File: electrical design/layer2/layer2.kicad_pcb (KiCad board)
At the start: 2 copper layers, 178 x 168.1 mm, 43 parts, among them J1 Conn_01x01_Female, J10 Conn_01x01_Female, J11 SH1.0 2P, J12 XT60-F, J13 XT60-F, J14 XH2.54 2P, J15 XT60-F, J16 XT60-F, J17 SH1.0 2P, J2 Conn_01x01_Female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

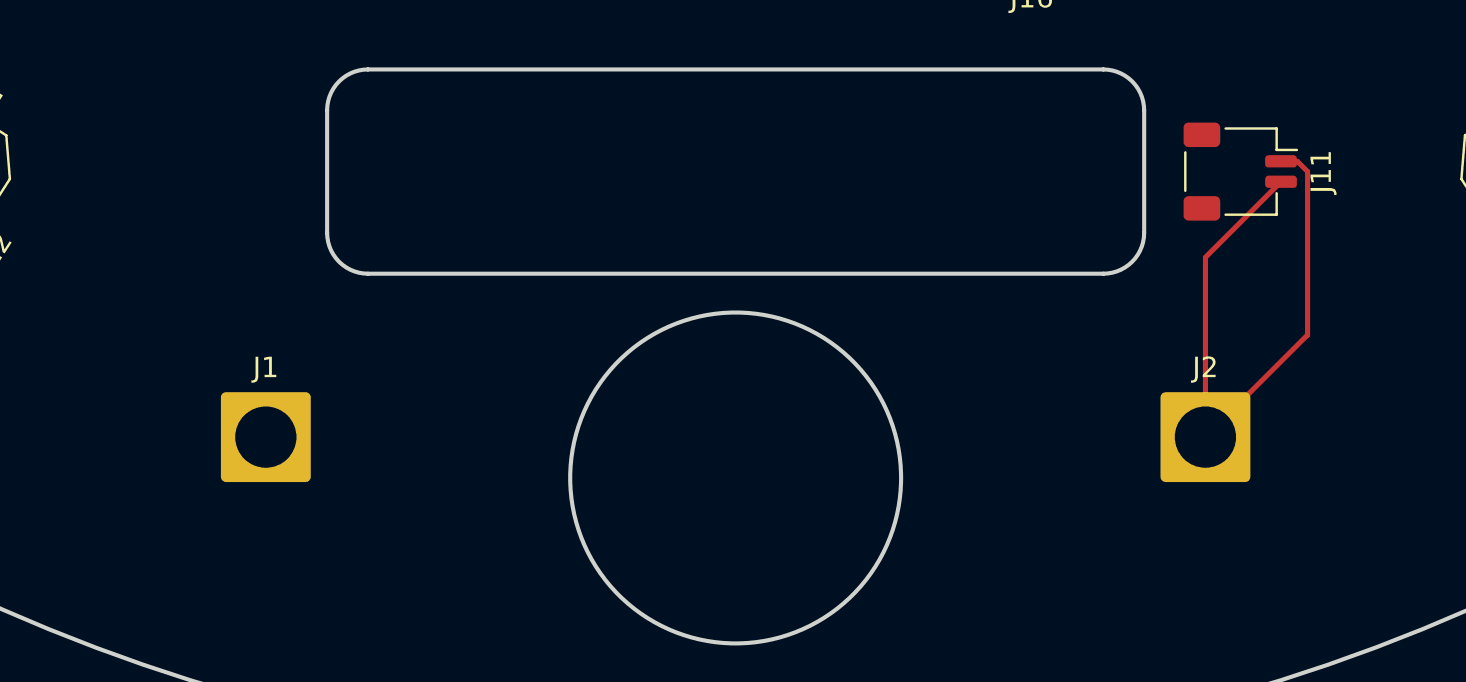
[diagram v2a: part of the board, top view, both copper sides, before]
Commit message: update l2 pcb with additional batt connectors
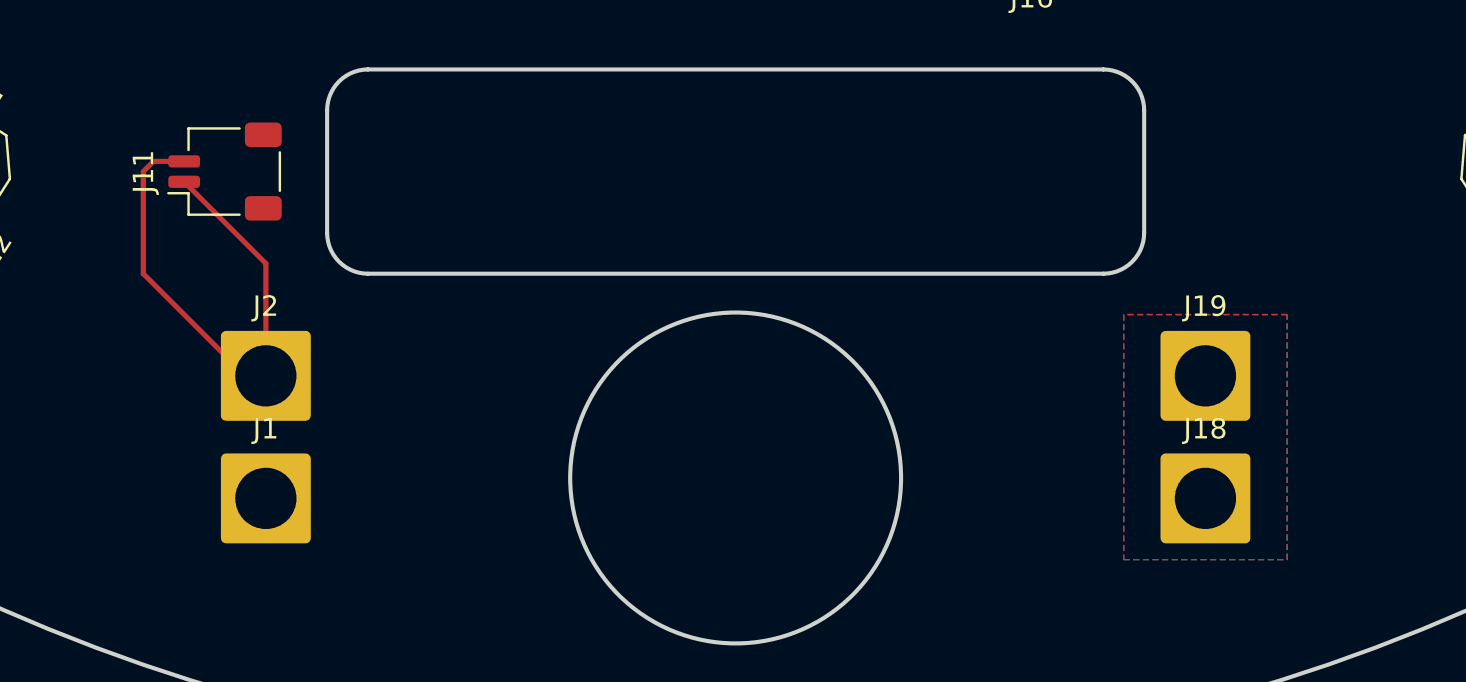
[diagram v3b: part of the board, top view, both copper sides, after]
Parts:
- added J18: Conn_01x01_Female, Connector_Wire:SolderWire-2.5sqmm_1x01_D2.4mm_OD4.4mm, F.Cu at (128.0, 181.0)
- added J19: Conn_01x01_Female, Connector_Wire:SolderWire-2.5sqmm_1x01_D2.4mm_OD4.4mm, F.Cu at (128.0, 175.0)
- moved J11 49.7 mm to (80.0, 165.0), turned to 90 degrees
- moved J2 46.1 mm to (82.0, 175.0)
- moved J1 3.00 mm to (82.0, 181.0)
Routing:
- net GND: track 32.0 -> 26.4 mm
- added copper zone on B.Cu, net /BATT
- added copper zone on F.Cu, net /BATT
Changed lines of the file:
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@@
   (net 1 "+12V")
   (net 2 "GND")
+  (net 3 "/BATT")
   (footprint "Connector_AMASS:AMASS_XT30UPB-F_1x02_P5.0mm_Vertical" (layer "F.Cu")
     (at 143.357043 164.747279 -57.3)
@@
   )
   (footprint "Connector_Wire:SolderWire-2.5sqmm_1x01_D2.4mm_OD4.4mm" (layer "F.Cu")
-    (at 128 178)
+    (at 128 181)
+    (descr "Soldered wire connection, for a single 2.5 mm² wire, reinforced insulation, conductor diameter 2.4mm, outer diameter 4.4mm, size source Multi-Contact FLEXI-xV 2.5 (https://ec.staubli.com/AcroFiles/Catalogues/TM_Cab-Main-11014119_(en)_hi.pdf), bend radius 3 times outer diameter, generated with kicad-footprint-generator")
+    (tags "connector wire 2.5sqmm")
+    (property "Sheetfile" "layer2.kicad_sch")
+    (property "Sheetname" "")
+    (property "ki_description" "Generic connector, single row, 01x01, script generated (kicad-library-utils/schlib/autogen/connector/)")
+    (property "ki_keywords" "connector")
+    (attr exclude_from_pos_files)
+    (fp_text reference "J18" (at 0 -3.4) (layer "F.SilkS")
+        (effects (font (size 1 1) (thickness 0.15)))
+    )
+    (fp_text value "Conn_01x01_Female" (at 0 3.4) (layer "F.Fab")
+        (effects (font (size 1 1) (thickness 0.15)))
+    )
+    (fp_text user "${REFERENCE}" (at 0 0) (layer "F.Fab")
+        (effects (font (size 1 1) (thickness 0.15)))
+    )
+    (fp_line (start -2.95 -2.7) (end -2.95 2.7)
+      (stroke (width 0.05) (type solid)) (layer "F.CrtYd"))
+    (fp_line (start -2.95 2.7) (end 2.95 2.7)
+      (stroke (width 0.05) (type solid)) (layer "F.CrtYd"))
+    (fp_line (start 2.95 -2.7) (end -2.95 -2.7)
+      (stroke (width 0.05) (type solid)) (layer "F.CrtYd"))
+    (fp_line (start 2.95 2.7) (end 2.95 -2.7)
+      (stroke (width 0.05) (type solid)) (layer "F.CrtYd"))
+    (fp_circle (center 0 0) (end 2.2 0)
+      (stroke (width 0.1) (type solid)) (fill none) (layer "F.Fab"))
+    (pad "1" thru_hole roundrect (at 0 0) (size 4.4 4.4) (drill 3) (layers "*.Cu" "*.Mask") (roundrect_rratio 0.056818)
+      (net 3 "/BATT") (pinfunction "Pin_1") (pintype "passive"))
+    (model "${KICAD6_3DMODEL_DIR}/Connector_Wire.3dshapes/SolderWire-2.5sqmm_1x01_D2.4mm_OD4.4mm.wrl"
+      (offset (xyz 0 0 0))
+      (scale (xyz 1 1 1))
+      (rotate (xyz 0 0 0))
+    )
+  )
+  (footprint "Connector_Wire:SolderWire-2.5sqmm_1x01_D2.4mm_OD4.4mm" (layer "F.Cu")
+    (at 82 175)
     (descr "Soldered wire connection, for a single 2.5 mm² wire, reinforced insulation, conductor diameter 2.4mm, outer diameter 4.4mm, size source Multi-Contact FLEXI-xV 2.5 (https://ec.staubli.com/AcroFiles/Catalogues/TM_Cab-Main-11014119_(en)_hi.pdf), bend radius 3 times outer diameter, generated with kicad-footprint-generator")
     (tags "connector wire 2.5sqmm")
@@
   )
   (footprint "Connector_JST:JST_SH_SM02B-SRSS-TB_1x02-1MP_P1.00mm_Horizontal" (layer "F.Cu")
-    (at 129.7 165 -90)
+    (at 80 165 90)
     (descr "JST SH series connector, SM02B-SRSS-TB (http://www.jst-mfg.com/product/pdf/eng/eSH.pdf), generated with kicad-footprint-generator")
     (tags "connector JST SH top entry")
@@
     (property "ki_keywords" "connector")
     (attr smd)
-    (fp_text reference "J11" (at 0 -3.98 -270) (layer "F.SilkS")
-        (effects (font (size 1 1) (thickness 0.15)))
-    )
-    (fp_text value "SH1.0 2P" (at 0 3.98 -270) (layer "F.Fab")
-        (effects (font (size 1 1) (thickness 0.15)))
-    )
-    (fp_text user "${REFERENCE}" (at 0 0 -270) (layer "F.Fab")
+    (fp_text reference "J11" (at 0 -3.98 90) (layer "F.SilkS")
+        (effects (font (size 1 1) (thickness 0.15)))
+    )
+    (fp_text value "SH1.0 2P" (at 0 3.98 90) (layer "F.Fab")
+        (effects (font (size 1 1) (thickness 0.15)))
+    )
+    (fp_text user "${REFERENCE}" (at 0 0 90) (layer "F.Fab")
         (effects (font (size 1 1) (thickness 0.15)))
     )
@@
     (fp_line (start 2 -1.675) (end 2 2.575)
       (stroke (width 0.1) (type solid)) (layer "F.Fab"))
-    (pad "1" smd roundrect (at -0.5 -2 270) (size 0.6 1.55) (layers "F.Cu" "F.Paste" "F.Mask") (roundrect_rratio 0.25)
+    (pad "1" smd roundrect (at -0.5 -2 90) (size 0.6 1.55) (layers "F.Cu" "F.Paste" "F.Mask") (roundrect_rratio 0.25)
       (net 2 "GND") (pinfunction "Pin_1") (pintype "passive"))
-    (pad "2" smd roundrect (at 0.5 -2 270) (size 0.6 1.55) (layers "F.Cu" "F.Paste" "F.Mask") (roundrect_rratio 0.25)
+    (pad "2" smd roundrect (at 0.5 -2 90) (size 0.6 1.55) (layers "F.Cu" "F.Paste" "F.Mask") (roundrect_rratio 0.25)
       (net 2 "GND") (pinfunction "Pin_2") (pintype "passive"))
-    (pad "MP" smd roundrect (at -1.8 1.875 270) (size 1.2 1.8) (layers "F.Cu" "F.Paste" "F.Mask") (roundrect_rratio 0.208333))
-    (pad "MP" smd roundrect (at 1.8 1.875 270) (size 1.2 1.8) (layers "F.Cu" "F.Paste" "F.Mask") (roundrect_rratio 0.208333))
+    (pad "MP" smd roundrect (at -1.8 1.875 90) (size 1.2 1.8) (layers "F.Cu" "F.Paste" "F.Mask") (roundrect_rratio 0.208333))
+    (pad "MP" smd roundrect (at 1.8 1.875 90) (size 1.2 1.8) (layers "F.Cu" "F.Paste" "F.Mask") (roundrect_rratio 0.208333))
     (model "${KICAD6_3DMODEL_DIR}/Connector_JST.3dshapes/JST_SH_SM02B-SRSS-TB_1x02-1MP_P1.00mm_Horizontal.step"
       (offset (xyz 0 1 0))
@@
       (stroke (width 0.05) (type solid)) (fill none) (layer "F.CrtYd"))
     (pad "1" thru_hole circle (at 0 0) (size 4.4 4.4) (drill 2.2) (layers "*.Cu" "*.Mask"))
+  )
+  (footprint "Connector_Wire:SolderWire-2.5sqmm_1x01_D2.4mm_OD4.4mm" (layer "F.Cu")
+    (at 128 175)
+    (descr "Soldered wire connection, for a single 2.5 mm² wire, reinforced insulation, conductor diameter 2.4mm, outer diameter 4.4mm, size source Multi-Contact FLEXI-xV 2.5 (https://ec.staubli.com/AcroFiles/Catalogues/TM_Cab-Main-11014119_(en)_hi.pdf), bend radius 3 times outer diameter, generated with kicad-footprint-generator")
+    (tags "connector wire 2.5sqmm")
+    (property "Sheetfile" "layer2.kicad_sch")
+    (property "Sheetname" "")
+    (property "ki_description" "Generic connector, single row, 01x01, script generated (kicad-library-utils/schlib/autogen/connector/)")
+    (property "ki_keywords" "connector")
+    (attr exclude_from_pos_files)
+    (fp_text reference "J19" (at 0 -3.4) (layer "F.SilkS")
+        (effects (font (size 1 1) (thickness 0.15)))
+    )
+    (fp_text value "Conn_01x01_Female" (at 0 3.4) (layer "F.Fab")
+        (effects (font (size 1 1) (thickness 0.15)))
+    )
+    (fp_text user "${REFERENCE}" (at 0 0) (layer "F.Fab")
+        (effects (font (size 1 1) (thickness 0.15)))
+    )
+    (fp_line (start -2.95 -2.7) (end -2.95 2.7)
+      (stroke (width 0.05) (type solid)) (layer "F.CrtYd"))
+    (fp_line (start -2.95 2.7) (end 2.95 2.7)
+      (stroke (width 0.05) (type solid)) (layer "F.CrtYd"))
+    (fp_line (start 2.95 -2.7) (end -2.95 -2.7)
+      (stroke (width 0.05) (type solid)) (layer "F.CrtYd"))
+    (fp_line (start 2.95 2.7) (end 2.95 -2.7)
+      (stroke (width 0.05) (type solid)) (layer "F.CrtYd"))
+    (fp_circle (center 0 0) (end 2.2 0)
+      (stroke (width 0.1) (type solid)) (fill none) (layer "F.Fab"))
+    (pad "1" thru_hole roundrect (at 0 0) (size 4.4 4.4) (drill 3) (layers "*.Cu" "*.Mask") (roundrect_rratio 0.056818)
+      (net 3 "/BATT") (pinfunction "Pin_1") (pintype "passive"))
+    (model "${KICAD6_3DMODEL_DIR}/Connector_Wire.3dshapes/SolderWire-2.5sqmm_1x01_D2.4mm_OD4.4mm.wrl"
+      (offset (xyz 0 0 0))
+      (scale (xyz 1 1 1))
+      (rotate (xyz 0 0 0))
+    )
   )
   (footprint "MountingHole:MountingHole_3.2mm_M3_Pad" (layer "F.Cu")
@@
   )
   (footprint "Connector_Wire:SolderWire-2.5sqmm_1x01_D2.4mm_OD4.4mm" (layer "F.Cu")
-    (at 82 178)
+    (at 82 181)
     (descr "Soldered wire connection, for a single 2.5 mm² wire, reinforced insulation, conductor diameter 2.4mm, outer diameter 4.4mm, size source Multi-Contact FLEXI-xV 2.5 (https://ec.staubli.com/AcroFiles/Catalogues/TM_Cab-Main-11014119_(en)_hi.pdf), bend radius 3 times outer diameter, generated with kicad-footprint-generator")
     (tags "connector wire 2.5sqmm")
@@
   (gr_line (start 158.048228 171.859363) (end 146.853507 162.465877)
     (stroke (width 0.2) (type solid)) (layer "Edge.Cuts"))
-  (segment (start 128 178) (end 128 169.2) (width 0.25) (layer "F.Cu") (net 2))
-  (segment (start 128.5 177.5) (end 128 178) (width 0.25) (layer "F.Cu") (net 2))
-  (segment (start 133 173) (end 128 178) (width 0.25) (layer "F.Cu") (net 2))
-  (segment (start 128 169.2) (end 131.7 165.5) (width 0.25) (layer "F.Cu") (net 2))
-  (segment (start 131.7 164.5) (end 132.5 164.5) (width 0.25) (layer "F.Cu") (net 2))
-  (segment (start 133 165) (end 133 173) (width 0.25) (layer "F.Cu") (net 2))
-  (segment (start 127.5 177.5) (end 128 178) (width 0.25) (layer "F.Cu") (net 2))
-  (segment (start 132.5 164.5) (end 133 165) (width 0.25) (layer "F.Cu") (net 2))
+  (segment (start 78 165.5) (end 82 169.5) (width 0.25) (layer "F.Cu") (net 2))
+  (segment (start 81 175) (end 82 175) (width 0.25) (layer "F.Cu") (net 2))
+  (segment (start 76.5 164.5) (end 76 165) (width 0.25) (layer "F.Cu") (net 2))
+  (segment (start 76 165) (end 76 170) (width 0.25) (layer "F.Cu") (net 2))
+  (segment (start 76 170) (end 81 175) (width 0.25) (layer "F.Cu") (net 2))
+  (segment (start 82 169.5) (end 82 175) (width 0.25) (layer "F.Cu") (net 2))
+  (segment (start 78 164.5) (end 76.5 164.5) (width 0.25) (layer "F.Cu") (net 2))
   (zone (net 1) (net_name "+12V") (layer "F.Cu") (hatch edge 0.508)
     (connect_pads (clearance 0.508))
@@
       )
     )
+  )
+  (zone (net 3) (net_name "/BATT") (layers "F&B.Cu") (hatch edge 0.5)
+    (priority 1)
+    (connect_pads (clearance 0.508))
+    (min_thickness 0.25) (filled_areas_thickness no)
+    (fill yes (thermal_gap 0.5) (thermal_bridge_width 0.5))
+    (polygon
+      (pts
+        (xy 124 184)
+        (xy 132 184)
+        (xy 132 172)
+        (xy 124 172)
+      )
+    )

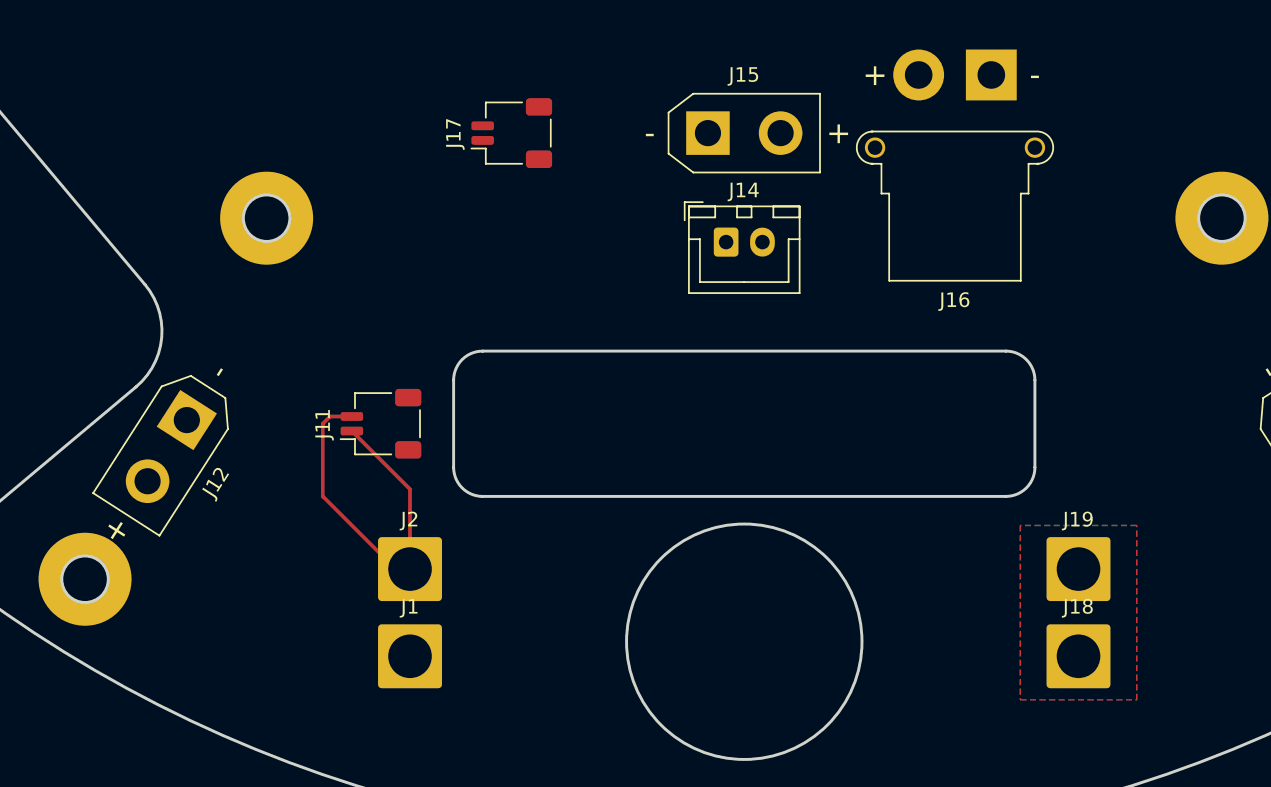
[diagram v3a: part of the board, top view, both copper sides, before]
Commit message: update pcbs for dual camera design
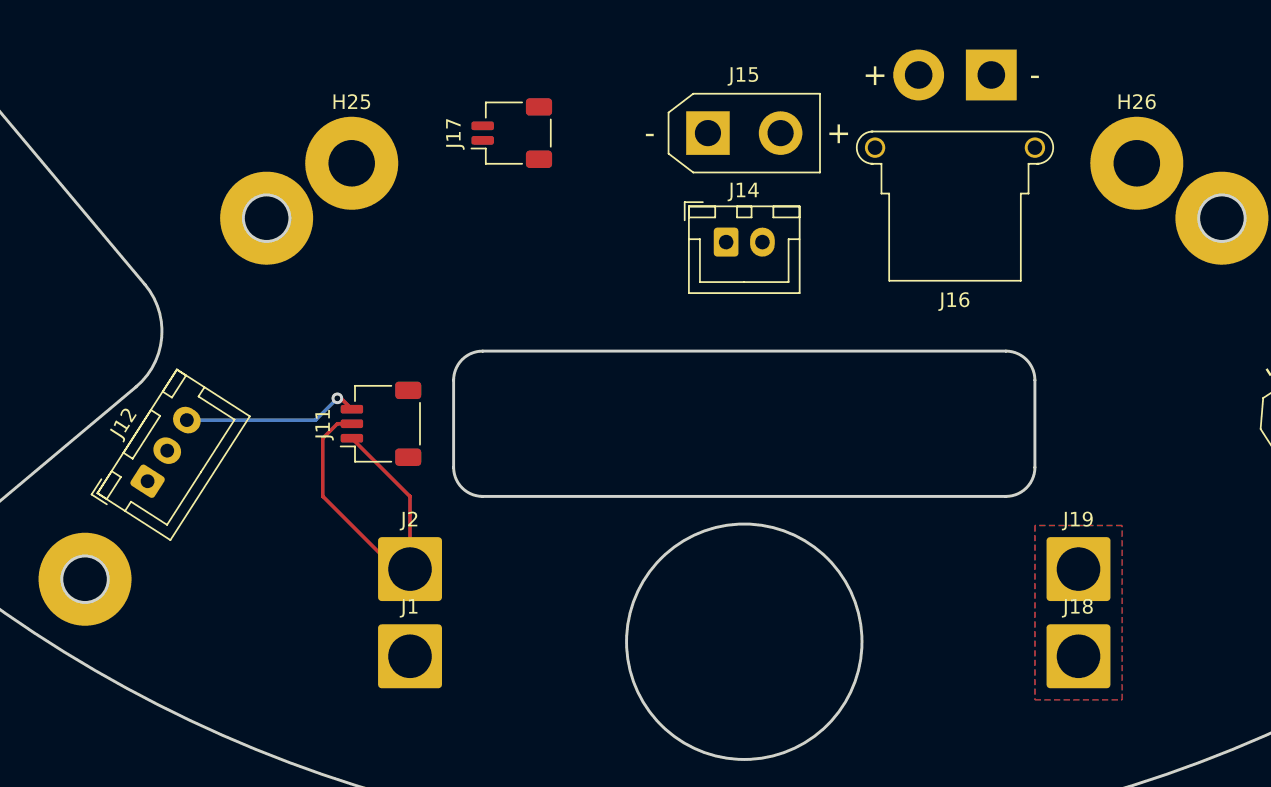
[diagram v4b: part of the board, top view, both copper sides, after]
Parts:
- added H25: MountingHole, MountingHole:MountingHole_3.2mm_M3_Pad, F.Cu at (78.0, 147.1)
- added H26: MountingHole, MountingHole:MountingHole_3.2mm_M3_Pad, F.Cu at (132.0, 147.1)
- J11: value SH1.0 2P -> SH1.0 3P; footprint Connector_JST:JST_SH_SM02B-SRSS-TB_1x02-1MP_P1.00mm_Horizontal -> Connector_JST:JST_SH_SM03B-SRSS-TB_1x03-1MP_P1.00mm_Horizontal
- J12: value XT60-F -> XH2.54 3P; footprint Connector_AMASS:AMASS_XT30UPB-F_1x02_P5.0mm_Vertical -> Connector_JST:JST_XH_B3B-XH-A_1x03_P2.50mm_Vertical
- moved J12 5.00 mm to (63.9, 169.0), turned to 57.301 degrees
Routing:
- net +3V3: track 0.00 -> 12.3 mm, vias 0 -> 1
- net GND: track 26.4 -> 25.1 mm
